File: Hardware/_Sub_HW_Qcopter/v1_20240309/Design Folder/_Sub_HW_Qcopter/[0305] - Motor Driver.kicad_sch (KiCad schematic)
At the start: 0 parts

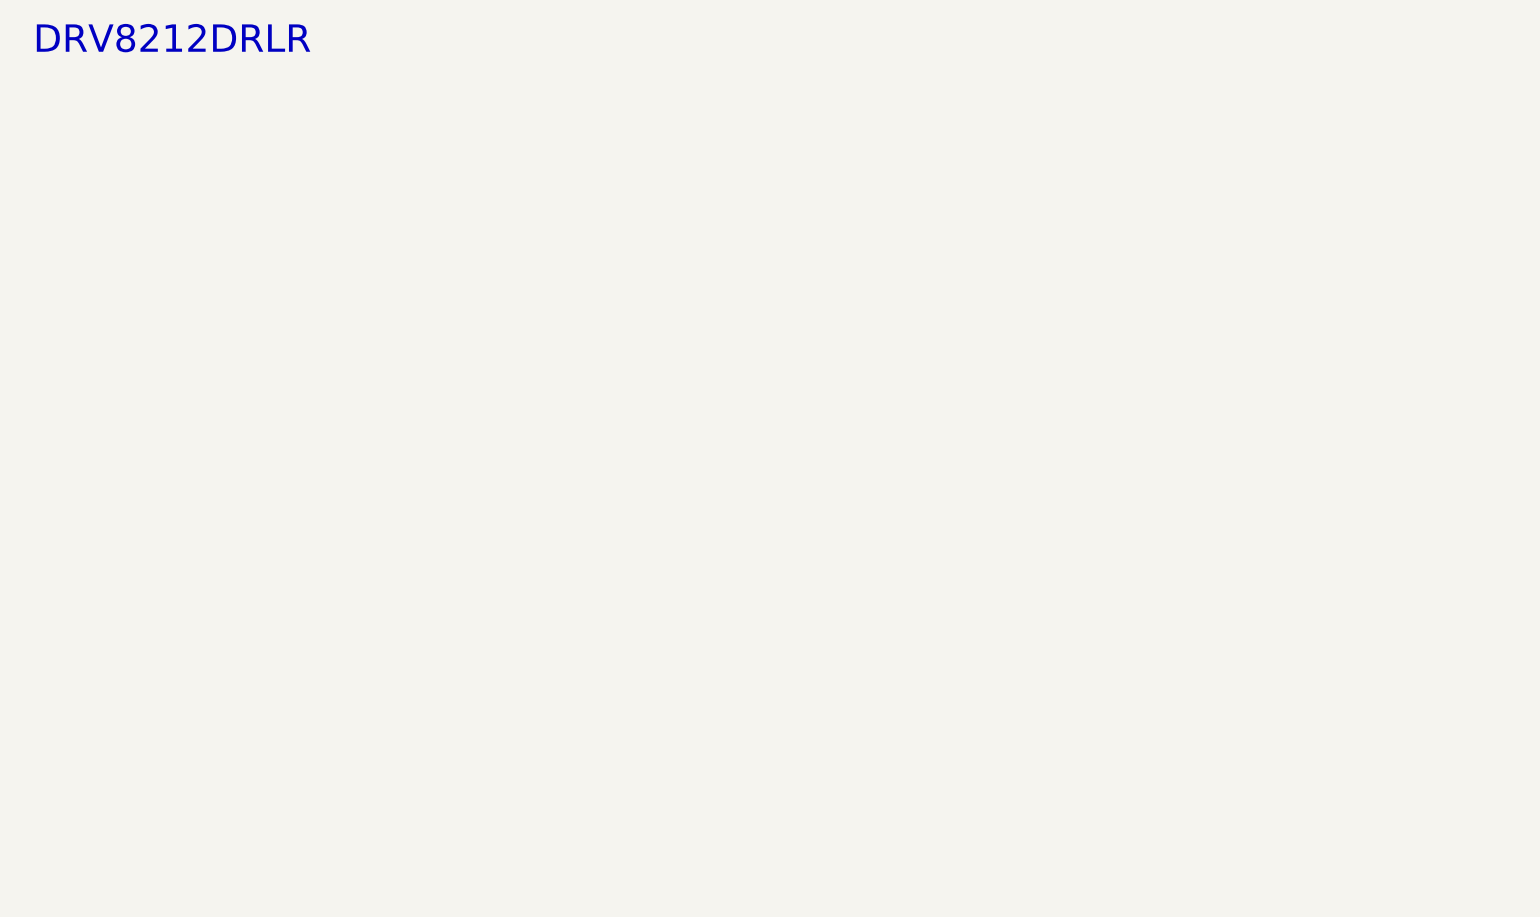
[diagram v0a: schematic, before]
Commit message: Schematic is done by 90%
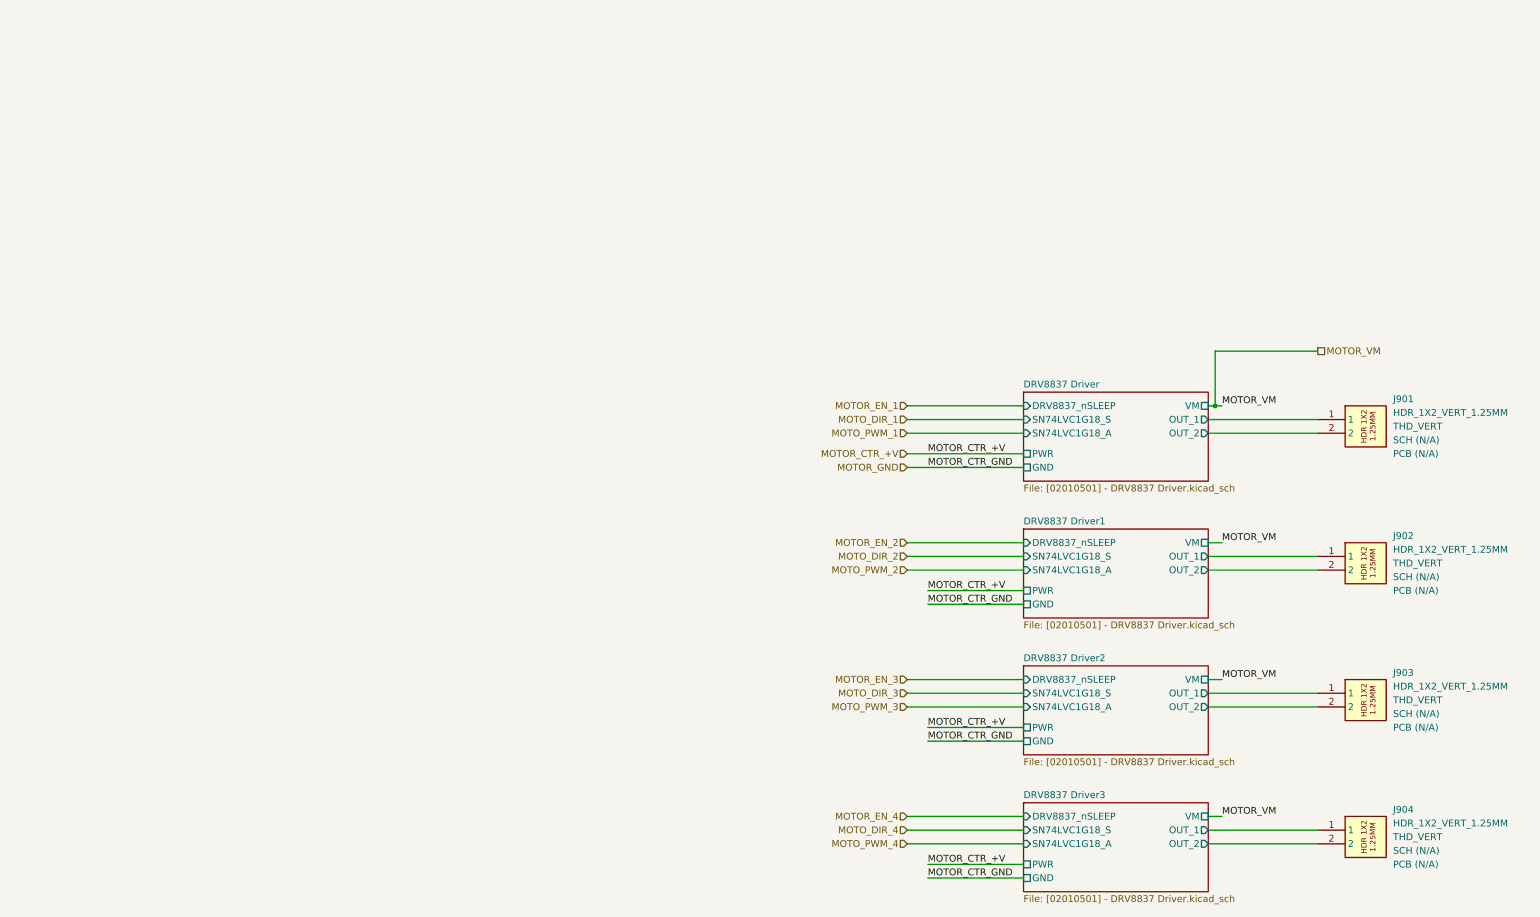
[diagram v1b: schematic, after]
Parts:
- added J901, J902, J903, J904: HDR_1X2_VERT_1.25MM, Connector_Hirose:Hirose_DF13-02P-1.25DSA_1x02_P1.25mm_Vertical, symbol _SCHLIB_Qcopter:CONN_HDR_1X2_VERT_THD-1.25MM
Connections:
- new net DRV8837 Driver/OUT_1: J901.1
- new net DRV8837 Driver/OUT_2: J901.2
- new net DRV8837 Driver1/OUT_1: J902.1
- new net DRV8837 Driver1/OUT_2: J902.2
- new net DRV8837 Driver2/OUT_1: J903.1
- new net DRV8837 Driver2/OUT_2: J903.2
- new net DRV8837 Driver3/OUT_1: J904.1
- new net DRV8837 Driver3/OUT_2: J904.2
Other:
- added sheet DRV8837 Driver ([02010501] - DRV8837 Driver.kicad_sch)
- added sheet DRV8837 Driver1 ([02010501] - DRV8837 Driver.kicad_sch)
- added sheet DRV8837 Driver2 ([02010501] - DRV8837 Driver.kicad_sch)
- added sheet DRV8837 Driver3 ([02010501] - DRV8837 Driver.kicad_sch)
- note removed: "DRV8212DRLR"
